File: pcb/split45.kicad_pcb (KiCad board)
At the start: 2 copper layers, 92 parts, among them U1 nice_nano, U2 nice_nano

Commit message: route the left side
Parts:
- moved D41 161.9 mm to (260.4, 64.3)
- moved D46 161.9 mm to (284.2, 26.2)
- moved D47 161.9 mm to (256.4, 45.2)
- moved D48 161.9 mm to (284.2, 64.3)
- moved MXR3,7 161.9 mm to (272.3, 64.3)
- moved MXR4,5 161.9 mm to (260.4, 83.3)
- moved D23 161.9 mm to (169.9, 26.2)
- moved D24 161.9 mm to (174.6, 45.2)
- moved D25 161.9 mm to (184.2, 64.3)
- moved D26 161.9 mm to (208.0, 83.3)
- moved D28 161.9 mm to (188.9, 26.2)
- moved D29 161.9 mm to (193.7, 45.2)
- moved D30 161.9 mm to (203.2, 64.3)
- moved D31 161.9 mm to (227.0, 83.3)
- moved D32 161.9 mm to (208.0, 26.2)
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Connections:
- U1 pad 10: Net-(U1-Pad10) -> LCol4
- U1 pad 11: Net-(U1-Pad11) -> LCol3
- U1 pad 12: Net-(U1-Pad12) -> LCol2
- U1 pad 19: Net-(U1-Pad19) -> LRow2
- U1 pad 20: Net-(U1-Pad20) -> LRow1
- U1 pad 5: Net-(U1-Pad5) -> LRow4
- U1 pad 6: Net-(U1-Pad6) -> LRow3
- U1 pad 7: Net-(U1-Pad7) -> LCol1
- U1 pad 8: Net-(U1-Pad8) -> LCol6
- U1 pad 9: Net-(U1-Pad9) -> LCol5
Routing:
- net LCol6: track 0.00 -> 198.5 mm
- net LCol5: track 0.00 -> 183.6 mm
- net LCol4: track 0.00 -> 161.3 mm
- net LRow3: track 0.00 -> 151.8 mm
- net LRow4: track 0.00 -> 148.0 mm
- net LCol3: track 0.00 -> 141.3 mm
- net LRow1: track 0.00 -> 113.7 mm
- net LRow2: track 0.00 -> 109.4 mm
- net LCol2: track 0.00 -> 81.9 mm
- net LCol1: track 0.00 -> 57.7 mm
- net Net-(D3-Pad2): track 0.00 -> 15.5 mm
- net Net-(D20-Pad2): track 0.00 -> 12.8 mm
- net Net-(D21-Pad2): track 0.00 -> 12.3 mm
- net Net-(D19-Pad2): track 0.00 -> 11.9 mm
- net Net-(D11-Pad2): track 0.00 -> 10.8 mm
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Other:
- board outline added: 270.7 x 166.7 mm

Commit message: right hand routing and fill areas
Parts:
- moved D48 22.2 mm to (261.9, 64.3)
- moved D46 17.5 mm to (266.7, 26.2)
- moved D42 17.5 mm to (252.4, 83.3)
- moved D41 1.59 mm to (258.8, 64.3)
- moved D43 1.59 mm to (263.5, 26.2)
- moved D38 1.59 mm to (249.2, 83.3)
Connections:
- D31 pad 1: Net-(D31-Pad1) -> RRow4
- D38 pad 1: Net-(D31-Pad1) -> RRow4
- D42 pad 1: Net-(D31-Pad1) -> RRow4
- U1 pad 23: Net-(U1-Pad23) -> GND
- U1 pad 3: Net-(U1-Pad3) -> GND
- U1 pad 4: Net-(U1-Pad4) -> GND
- U2 pad 14: Net-(U2-Pad14) -> RCol5
- U2 pad 15: Net-(U2-Pad15) -> RCol4
- U2 pad 16: Net-(U2-Pad16) -> RCol3
- U2 pad 17: Net-(U2-Pad17) -> RCol2
- U2 pad 18: Net-(U2-Pad18) -> RCol1
- U2 pad 19: Net-(U2-Pad19) -> RRow3
- U2 pad 20: Net-(U2-Pad20) -> RRow4
- U2 pad 23: Net-(U2-Pad23) -> RGND
- U2 pad 3: Net-(U2-Pad3) -> RGND
- U2 pad 4: Net-(U2-Pad4) -> RGND
- U2 pad 5: Net-(U2-Pad5) -> RRow1
- U2 pad 6: Net-(U2-Pad6) -> RRow2
- U2 pad 7: Net-(U2-Pad7) -> RCol7
- U2 pad 8: Net-(U2-Pad8) -> RCol6
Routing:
- net RCol1: track 0.00 -> 249.5 mm
- net RCol2: track 0.00 -> 221.6 mm
- net RCol3: track 0.00 -> 208.6 mm
- net RCol4: track 0.00 -> 193.6 mm
- net RCol5: track 0.00 -> 176.9 mm
- net RRow3: track 0.00 -> 144.4 mm
- net RRow1: track 0.00 -> 138.3 mm
- net RRow4: track 0.00 -> 123.4 mm
- net RRow2: track 0.00 -> 121.1 mm
- net RCol7: track 0.00 -> 71.1 mm
- net RCol6: track 0.00 -> 25.9 mm
- net Net-(D26-Pad2): track 0.00 -> 25.1 mm
- net LCol4: track 161.3 -> 180.4 mm
- net LCol5: track 183.6 -> 202.0 mm
- net LCol6: track 198.5 -> 215.8 mm
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- added copper zone on B.Cu, net GND
- added copper zone on F.Cu, net GND
- added copper zone on B.Cu, net RGND
- added copper zone on F.Cu, net RGND

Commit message: add reset pads
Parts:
- added GND1: Conn_01x01_Female, Connector_Wire:SolderWire-0.15sqmm_1x01_D0.5mm_OD1.5mm, F.Cu at (26.4, 63.0)
- added RGND1: Conn_01x01_Female, Connector_Wire:SolderWire-0.15sqmm_1x01_D0.5mm_OD1.5mm, F.Cu at (276.4, 43.8)
- added RReset1: Conn_01x01_Female, Connector_Wire:SolderWire-0.15sqmm_1x01_D0.5mm_OD1.5mm, F.Cu at (276.4, 46.6)
- added Reset1: Conn_01x01_Female, Connector_Wire:SolderWire-0.15sqmm_1x01_D0.5mm_OD1.5mm, F.Cu at (26.4, 65.8)
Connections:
- U2 pad 22: Net-(U2-Pad22) -> RGND
- U2 pad 23: RGND -> Net-(U2-Pad23)
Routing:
- net Net-(Reset1-Pad1): track 0.00 -> 33.0 mm
- net Net-(RReset1-Pad1): track 0.00 -> 8.28 mm
- net LRow4: track 148.0 -> 145.4 mm
- net LRow3: track 151.8 -> 150.7 mm

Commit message: move holes in base, add images and text to pcb
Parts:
- added G***: LOGO, split45:rightpaw, F.Cu at (278.6, 82.5)
- added G***: LOGO, split45:leftpaw, F.Cu at (24.6, 82.5)
- added G***: LOGO, split45:leftpaw, F.Cu at (67.5, 127.0)
- added G***: LOGO, split45:leftpaw, F.Cu at (46.0, 104.0)
- added G***: LOGO, split45:leftpaw, F.Cu at (43.7, 100.0)
- added REF**: MountingHole_2.2mm_M2, MountingHole:MountingHole_2.2mm_M2, F.Cu at (23.8, 100.8)
- added REF**: MountingHole_2.2mm_M2, MountingHole:MountingHole_2.2mm_M2, F.Cu at (146.8, 147.6)
- added REF**: MountingHole_2.2mm_M2, MountingHole:MountingHole_2.2mm_M2, F.Cu at (132.6, 17.8)
- added REF**: MountingHole_2.2mm_M2, MountingHole:MountingHole_2.2mm_M2, F.Cu at (146.8, 55.6)
- added REF**: MountingHole_2.2mm_M2, MountingHole:MountingHole_2.2mm_M2, F.Cu at (165.9, 55.6)
- added REF**: MountingHole_2.2mm_M2, MountingHole:MountingHole_2.2mm_M2, F.Cu at (151.6, 17.8)
- added REF**: MountingHole_2.2mm_M2, MountingHole:MountingHole_2.2mm_M2, F.Cu at (283.4, 17.8)
- added REF**: MountingHole_2.2mm_M2, MountingHole:MountingHole_2.2mm_M2, F.Cu at (282.6, 91.3)
- added REF**: MountingHole_2.2mm_M2, MountingHole:MountingHole_2.2mm_M2, F.Cu at (157.2, 91.3)
- added REF**: MountingHole_2.2mm_M2, MountingHole:MountingHole_2.2mm_M2, F.Cu at (136.5, 91.3)
- added REF**: MountingHole_2.2mm_M2, MountingHole:MountingHole_2.2mm_M2, F.Cu at (19.8, 17.5)
- added REF**: MountingHole_2.2mm_M2, MountingHole:MountingHole_2.2mm_M2, F.Cu at (128.6, 101.1)
- added REF**: MountingHole_2.2mm_M2, MountingHole:MountingHole_2.2mm_M2, F.Cu at (20.6, 91.3)
- added REF**: MountingHole_2.2mm_M2, MountingHole:MountingHole_2.2mm_M2, F.Cu at (161.1, 174.6)
- added REF**: MountingHole_2.2mm_M2, MountingHole:MountingHole_2.2mm_M2, F.Cu at (165.9, 147.6)
- added REF**: MountingHole_2.2mm_M2, MountingHole:MountingHole_2.2mm_M2, F.Cu at (155.6, 100.8)
- added REF**: MountingHole_2.2mm_M2, MountingHole:MountingHole_2.2mm_M2, F.Cu at (24.6, 174.6)
- added REF**: MountingHole_2.2mm_M2, MountingHole:MountingHole_2.2mm_M2, F.Cu at (132.6, 174.6)
- added REF**: MountingHole_2.2mm_M2, MountingHole:MountingHole_2.2mm_M2, F.Cu at (279.4, 100.8)
- added REF**: MountingHole_2.2mm_M2, MountingHole:MountingHole_2.2mm_M2, F.Cu at (278.6, 174.6)
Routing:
- net RCol1: track 249.5 -> 252.2 mm
- added copper zone on B.Cu, net (none)
- added copper zone on F.Cu, net (none)
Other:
- board size 270.7 x 166.7 mm -> 269.9 x 164.3 mm
- board text added: "for your left paw"
- board text added: "for your right paw"
- board text added: "thesplitfortyfive v0.1"
- board text added: "with love from Old Badger"

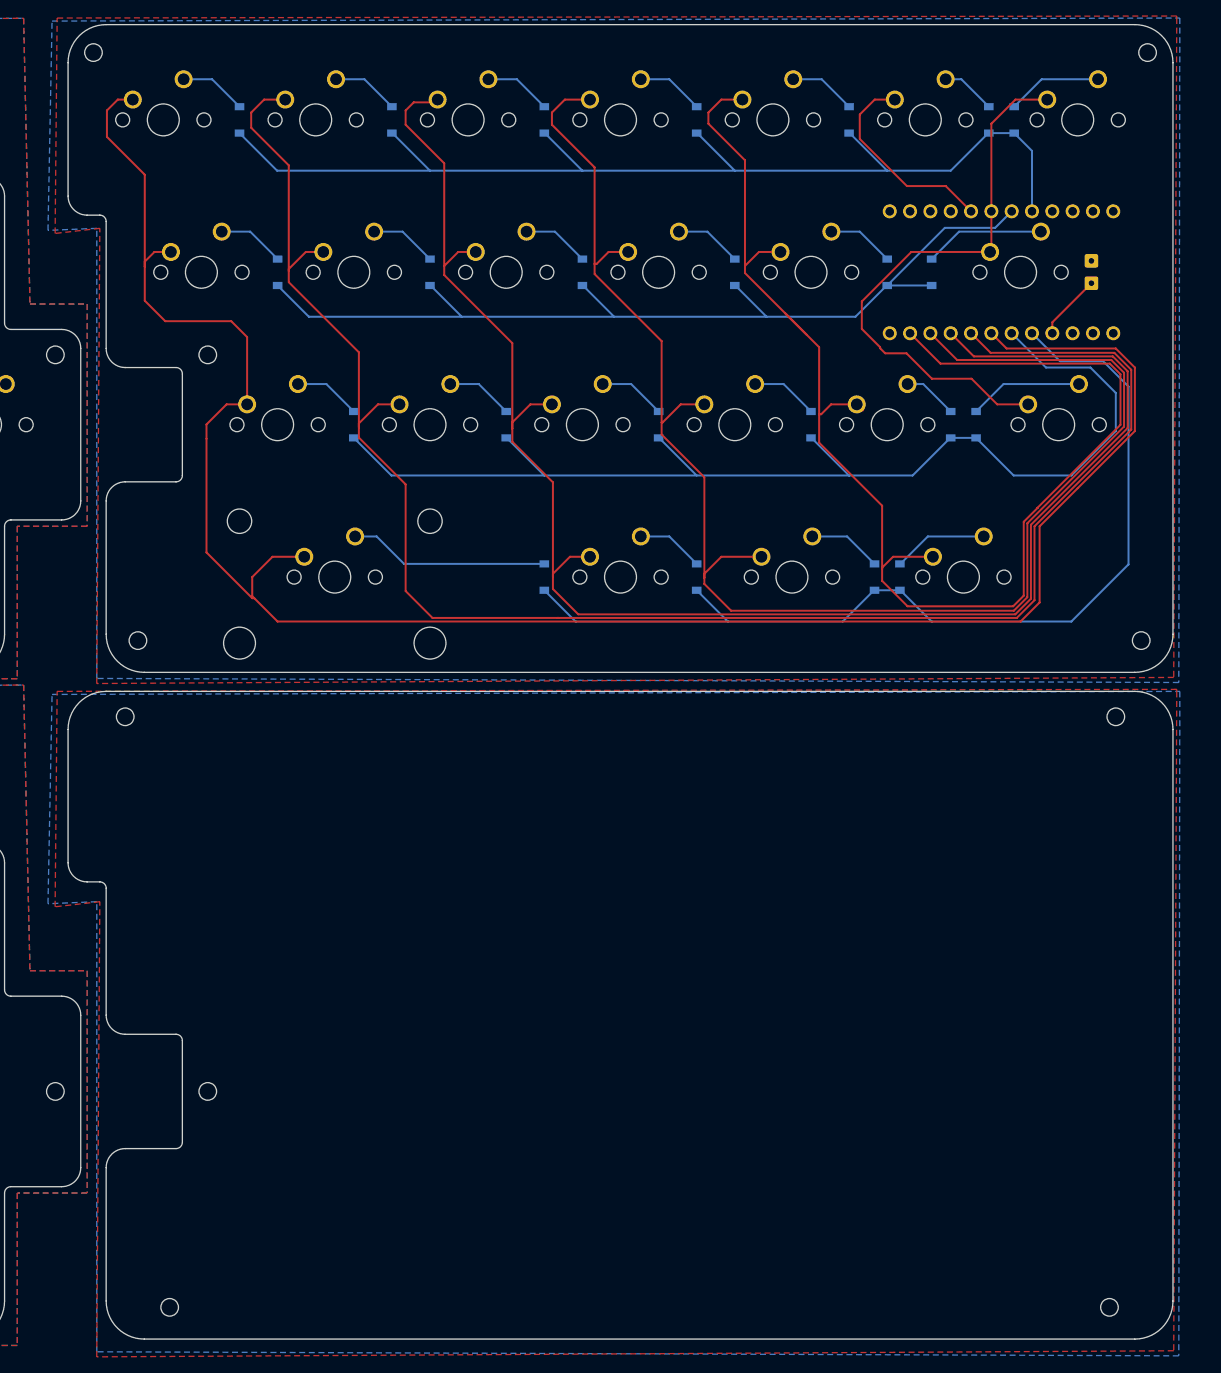
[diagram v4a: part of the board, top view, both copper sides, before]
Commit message: tweak position of boards on page
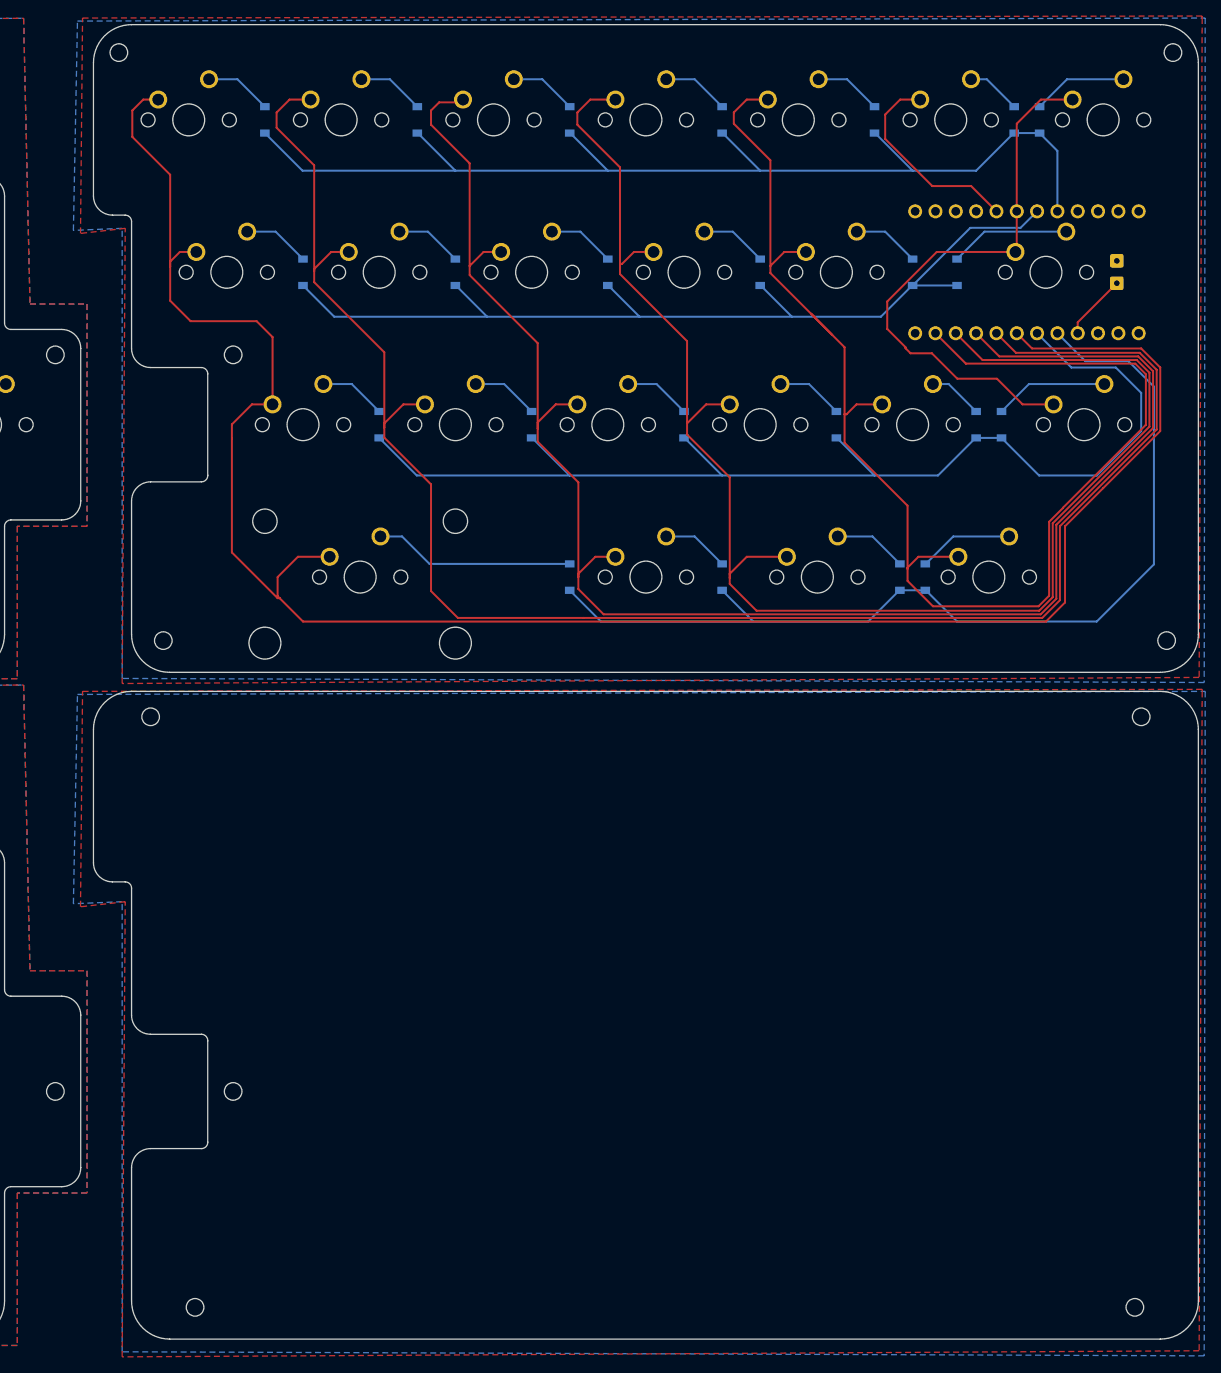
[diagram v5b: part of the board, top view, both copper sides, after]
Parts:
- removed the REF** at (165.9, 55.6)
- removed the REF** at (151.6, 17.8)
- removed the REF** at (283.4, 17.8)
- removed the REF** at (282.6, 91.3)
- removed the REF** at (157.2, 91.3)
- removed the REF** at (161.1, 174.6)
- removed the REF** at (165.9, 147.6)
- removed the REF** at (155.6, 100.8)
- removed the REF** at (279.4, 100.8)
- removed the REF** at (278.6, 174.6)
- added REF**: MountingHole_2.2mm_M2, MountingHole:MountingHole_2.2mm_M2, F.Cu at (169.1, 55.6)
- added REF**: MountingHole_2.2mm_M2, MountingHole:MountingHole_2.2mm_M2, F.Cu at (154.8, 17.8)
- added REF**: MountingHole_2.2mm_M2, MountingHole:MountingHole_2.2mm_M2, F.Cu at (286.5, 17.8)
- added REF**: MountingHole_2.2mm_M2, MountingHole:MountingHole_2.2mm_M2, F.Cu at (285.8, 91.3)
- added REF**: MountingHole_2.2mm_M2, MountingHole:MountingHole_2.2mm_M2, F.Cu at (160.3, 91.3)
- added REF**: MountingHole_2.2mm_M2, MountingHole:MountingHole_2.2mm_M2, F.Cu at (164.3, 174.6)
- added REF**: MountingHole_2.2mm_M2, MountingHole:MountingHole_2.2mm_M2, F.Cu at (169.1, 147.6)
- added REF**: MountingHole_2.2mm_M2, MountingHole:MountingHole_2.2mm_M2, F.Cu at (158.8, 100.8)
- added REF**: MountingHole_2.2mm_M2, MountingHole:MountingHole_2.2mm_M2, F.Cu at (282.6, 100.8)
- added REF**: MountingHole_2.2mm_M2, MountingHole:MountingHole_2.2mm_M2, F.Cu at (281.8, 174.6)
- moved D24 3.18 mm to (177.8, 45.2)
- moved D28 3.18 mm to (192.1, 26.2)
- moved D30 3.18 mm to (206.4, 64.3)
- moved D31 3.18 mm to (230.2, 83.3)
- moved D33 3.18 mm to (215.9, 45.2)
- moved D34 3.18 mm to (225.4, 64.3)
- moved D35 3.18 mm to (230.2, 26.2)
- moved D39 3.18 mm to (249.2, 26.2)
- moved D40 3.18 mm to (254.0, 45.2)
- moved D41 3.18 mm to (261.9, 64.3)
- moved D42 3.18 mm to (255.6, 83.3)
- moved D43 3.18 mm to (266.7, 26.2)
- moved D46 3.18 mm to (269.9, 26.2)
- moved D48 3.18 mm to (265.1, 64.3)
- moved G*** 3.18 mm to (281.8, 82.5)
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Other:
- board size 269.9 x 164.3 mm -> 273.1 x 164.3 mm
